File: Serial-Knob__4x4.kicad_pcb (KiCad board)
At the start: 2 copper layers, 49 x 49 mm, 108 parts, among them IC1 ATTINY85-S, P1 CONN_4

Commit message: Changed the break-away tabs for the 4x4 panel.
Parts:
- removed the 1PIN at (113.0, 82.5)
- removed the 1PIN at (125.0, 45.0)
- removed the 1PIN at (113.0, 33.0)
- removed the 1PIN at (75.5, 45.0)
- removed the 1PIN at (87.5, 33.0)
- removed the 1PIN at (113.8, 57.0)
- removed the 1PIN at (87.5, 82.5)
- removed the 1PIN at (125.0, 45.8)
- removed the 1PIN at (113.8, 33.0)
- removed the 1PIN at (125.0, 44.2)
- removed the 1PIN at (112.2, 57.0)
- removed the 1PIN at (112.2, 33.0)
- removed the 1PIN at (86.8, 33.0)
- removed the 1PIN at (88.2, 33.0)
- removed the 1PIN at (125.0, 70.5)
- removed the 1PIN at (75.5, 44.2)
- removed the 1PIN at (75.5, 45.8)
- removed the 1PIN at (88.2, 82.5)
- removed the 1PIN at (75.5, 71.2)
- removed the 1PIN at (75.5, 69.8)
- removed the 1PIN at (99.5, 71.2)
- removed the 1PIN at (99.5, 69.8)
- removed the 1PIN at (86.8, 82.5)
- removed the 1PIN at (101.0, 70.5)
- removed the 1PIN at (112.2, 58.5)
- removed the 1PIN at (112.2, 82.5)
- removed the 1PIN at (125.0, 69.8)
- removed the 1PIN at (113.8, 58.5)
- removed the 1PIN at (125.0, 71.2)
- removed the 1PIN at (101.0, 69.8)
- removed the 1PIN at (101.0, 71.2)
- removed the 1PIN at (113.8, 82.5)
- removed the 1PIN at (99.5, 70.5)
- removed the 1PIN at (75.5, 70.5)
- removed the 1PIN at (113.0, 58.5)
- removed the 1PIN at (113.0, 57.0)
- added 1PIN: P***, 1pin, F.Cu at (106.5, 58.5)
- added 1PIN: P***, 1pin, F.Cu at (119.5, 57.0)
- added 1PIN: P***, 1pin, F.Cu at (119.5, 58.5)
- added 1PIN: P***, 1pin, F.Cu at (118.0, 58.5)
- added 1PIN: P***, 1pin, F.Cu at (92.5, 58.5)
- added 1PIN: P***, 1pin, F.Cu at (94.0, 58.5)
- added 1PIN: P***, 1pin, F.Cu at (94.0, 57.0)
- added 1PIN: P***, 1pin, F.Cu at (92.5, 57.0)
- added 1PIN: P***, 1pin, F.Cu at (93.2, 57.0)
- added 1PIN: P***, 1pin, F.Cu at (93.2, 58.5)
- added 1PIN: P***, 1pin, F.Cu at (99.5, 65.5)
- added 1PIN: P***, 1pin, F.Cu at (108.0, 58.5)
- added 1PIN: P***, 1pin, F.Cu at (99.5, 64.0)
- added 1PIN: P***, 1pin, F.Cu at (101.0, 64.0)
- added 1PIN: P***, 1pin, F.Cu at (101.0, 65.5)
- added 1PIN: P***, 1pin, F.Cu at (99.5, 64.8)
- added 1PIN: P***, 1pin, F.Cu at (101.0, 64.8)
- added 1PIN: P***, 1pin, F.Cu at (101.0, 76.2)
- added 1PIN: P***, 1pin, F.Cu at (99.5, 76.2)
- added 1PIN: P***, 1pin, F.Cu at (101.0, 77.0)
- added 1PIN: P***, 1pin, F.Cu at (101.0, 75.5)
- added 1PIN: P***, 1pin, F.Cu at (99.5, 75.5)
- added 1PIN: P***, 1pin, F.Cu at (108.0, 57.0)
- added 1PIN: P***, 1pin, F.Cu at (99.5, 77.0)
- added 1PIN: P***, 1pin, F.Cu at (99.5, 51.5)
- added 1PIN: P***, 1pin, F.Cu at (99.5, 50.0)
- added 1PIN: P***, 1pin, F.Cu at (101.0, 50.0)
- added 1PIN: P***, 1pin, F.Cu at (101.0, 51.5)
- added 1PIN: P***, 1pin, F.Cu at (99.5, 50.8)
- added 1PIN: P***, 1pin, F.Cu at (101.0, 50.8)
- added 1PIN: P***, 1pin, F.Cu at (106.5, 57.0)
- added 1PIN: P***, 1pin, F.Cu at (107.2, 57.0)
- added 1PIN: P***, 1pin, F.Cu at (107.2, 58.5)
- added 1PIN: P***, 1pin, F.Cu at (118.8, 58.5)
- added 1PIN: P***, 1pin, F.Cu at (118.8, 57.0)
- added 1PIN: P***, 1pin, F.Cu at (118.0, 57.0)
- moved 1PIN 5.75 mm to (81.8, 58.5)
- moved 1PIN 5.75 mm to (81.8, 57.0)
- moved 1PIN 5.75 mm to (101.0, 39.2)
- moved 1PIN 5.75 mm to (99.5, 39.2)
- moved 1PIN 5.75 mm to (101.0, 40.0)
- moved 1PIN 5.75 mm to (101.0, 38.5)
- moved 1PIN 5.75 mm to (81.0, 57.0)
- moved 1PIN 5.75 mm to (99.5, 38.5)
- moved 1PIN 5.75 mm to (99.5, 40.0)
- moved 1PIN 5.75 mm to (82.5, 57.0)
- moved 1PIN 5.75 mm to (82.5, 58.5)
- moved 1PIN 5.75 mm to (81.0, 58.5)

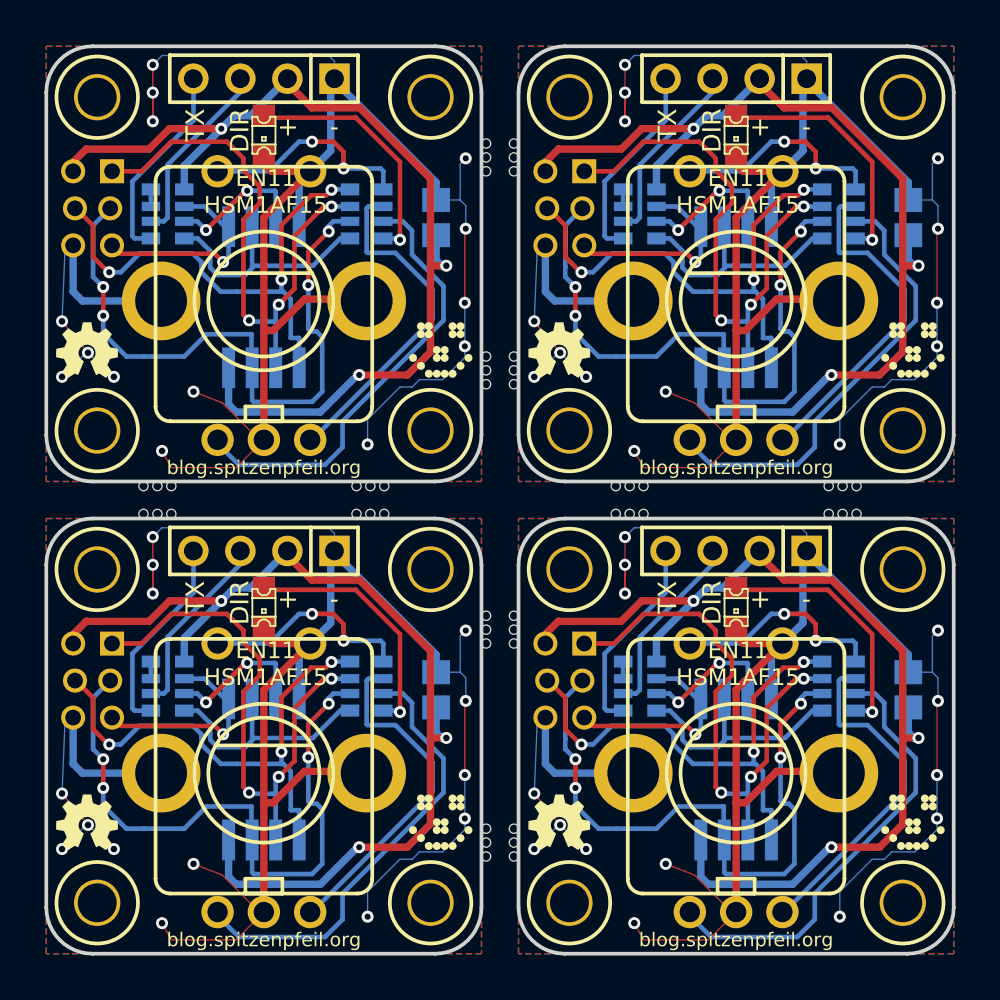
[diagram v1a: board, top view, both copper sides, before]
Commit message: Forgot board ID + date on 4x4 panel.
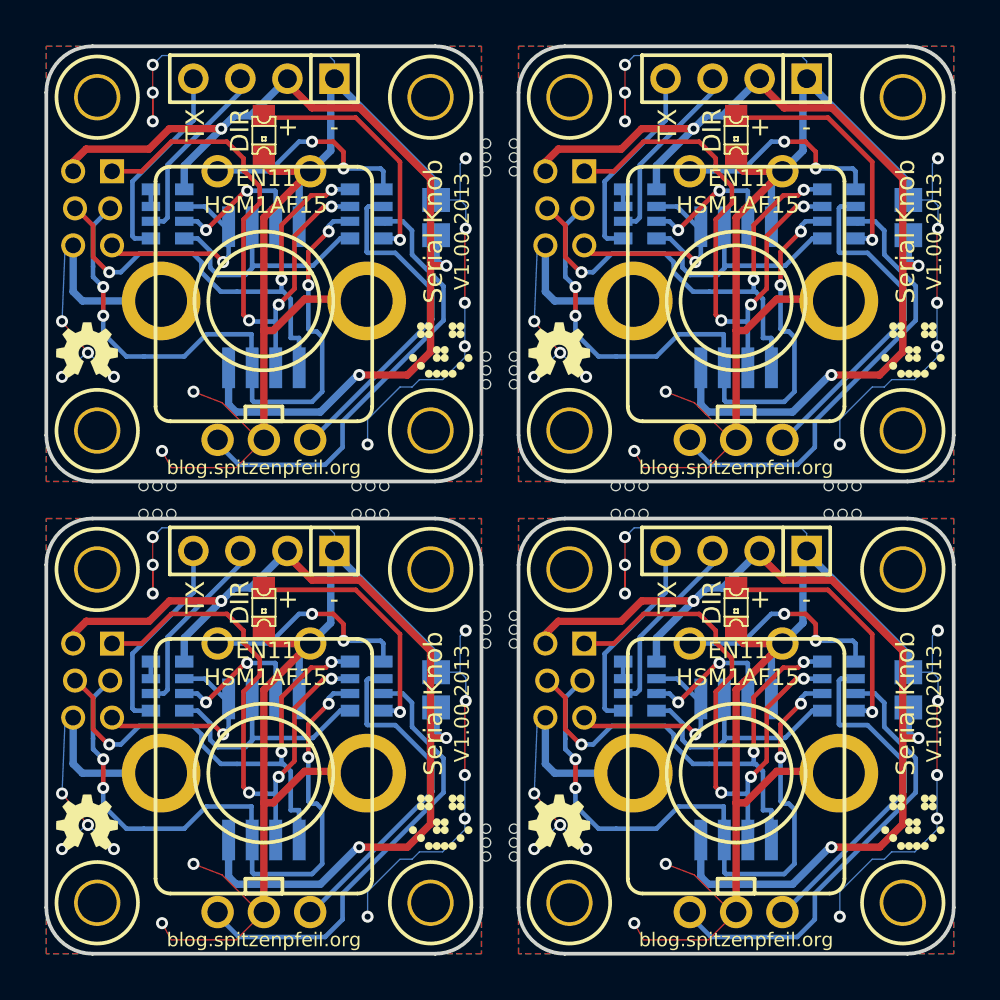
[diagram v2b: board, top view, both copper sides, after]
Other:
- board text added: "Serial Knob"
- board text added: "V1.00 2013"
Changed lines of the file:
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@@
     (links 165)
     (no_connects 45)
-    (area 73.616667 31.249999 126.750001 84.250001)
+    (area 73.616667 31.249999 127.304763 84.250001)
     (thickness 1.6002)
-    (drawings 132)
+    (drawings 140)
     (tracks 1068)
     (zones 0)
@@
   (layers
     (15 Front signal)
-    (0 Back signal hide)
+    (0 Back signal)
     (20 B.SilkS user)
     (21 F.SilkS user)
@@
   )
   (setup
-    (last_trace_width 0.18)
+    (last_trace_width 0.25)
     (user_trace_width 0.01)
     (user_trace_width 0.18)
@@
     )
   )
+  (gr_text "V1.00 2013" (at 123.7 68.75 90) (layer F.SilkS)
+    (effects (font (size 0.8 0.8) (thickness 0.2)))
+  )
+  (gr_text "Serial Knob" (at 122.15 68.75 90) (layer F.SilkS)
+    (effects (font (size 1 1) (thickness 0.2)))
+  )
+  (gr_text "Serial Knob" (at 96.65 68.75 90) (layer F.SilkS)
+    (effects (font (size 1 1) (thickness 0.2)))
+  )
+  (gr_text "V1.00 2013" (at 98.2 68.75 90) (layer F.SilkS)
+    (effects (font (size 0.8 0.8) (thickness 0.2)))
+  )
+  (gr_text "Serial Knob" (at 122.15 43.25 90) (layer F.SilkS)
+    (effects (font (size 1 1) (thickness 0.2)))
+  )
+  (gr_text "V1.00 2013" (at 123.7 43.25 90) (layer F.SilkS)
+    (effects (font (size 0.8 0.8) (thickness 0.2)))
+  )
+  (gr_text "V1.00 2013" (at 98.2 43.25 90) (layer F.SilkS)
+    (effects (font (size 0.8 0.8) (thickness 0.2)))
+  )
+  (gr_text "Serial Knob" (at 96.65 43.25 90) (layer F.SilkS)
+    (effects (font (size 1 1) (thickness 0.2)))
+  )
   (gr_line (start 105.25 57.75) (end 103.75 57.75) (angle 90) (layer Eco1.User) (width 2))

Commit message: Replaced all the NPTH holes with "mouse-byte" footprints.
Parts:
- removed 1PIN (x48): P***, 1pin
- added mouse-byte-2mm: VAL**, MADW__mouse-byte-2mm-slot, F.Cu at (100.2, 50.8)
- added mouse-byte-2mm: VAL**, MADW__mouse-byte-2mm-slot, F.Cu at (81.8, 57.8)
- added mouse-byte-2mm: VAL**, MADW__mouse-byte-2mm-slot, F.Cu at (93.2, 57.8)
- added mouse-byte-2mm: VAL**, MADW__mouse-byte-2mm-slot, F.Cu at (107.2, 57.8)
- added mouse-byte-2mm: VAL**, MADW__mouse-byte-2mm-slot, F.Cu at (118.8, 57.8)
- added mouse-byte-2mm: VAL**, MADW__mouse-byte-2mm-slot, F.Cu at (100.2, 64.8)
- added mouse-byte-2mm: VAL**, MADW__mouse-byte-2mm-slot, F.Cu at (100.2, 76.2)
- added mouse-byte-2mm: VAL**, MADW__mouse-byte-2mm-slot, F.Cu at (100.2, 39.2)

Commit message: Fixed a typo.
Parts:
- mouse-bite-2mm (x8): renamed from mouse-byte-2mm; footprint MADW__mouse-byte-2mm-slot -> MADW__mouse-bite-2mm-slot
